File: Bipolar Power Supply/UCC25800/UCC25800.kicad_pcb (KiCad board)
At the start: 2 copper layers, 70 x 50 mm, 71 parts, among them J1 1715721, J2 1715734, T1 750319331, U1 UCC25800-Q1, U2 LT8330_S6, U4 LT8330_S6, U5 LM317EMPX/NOPB, U6 LM337IMPX/NOPB

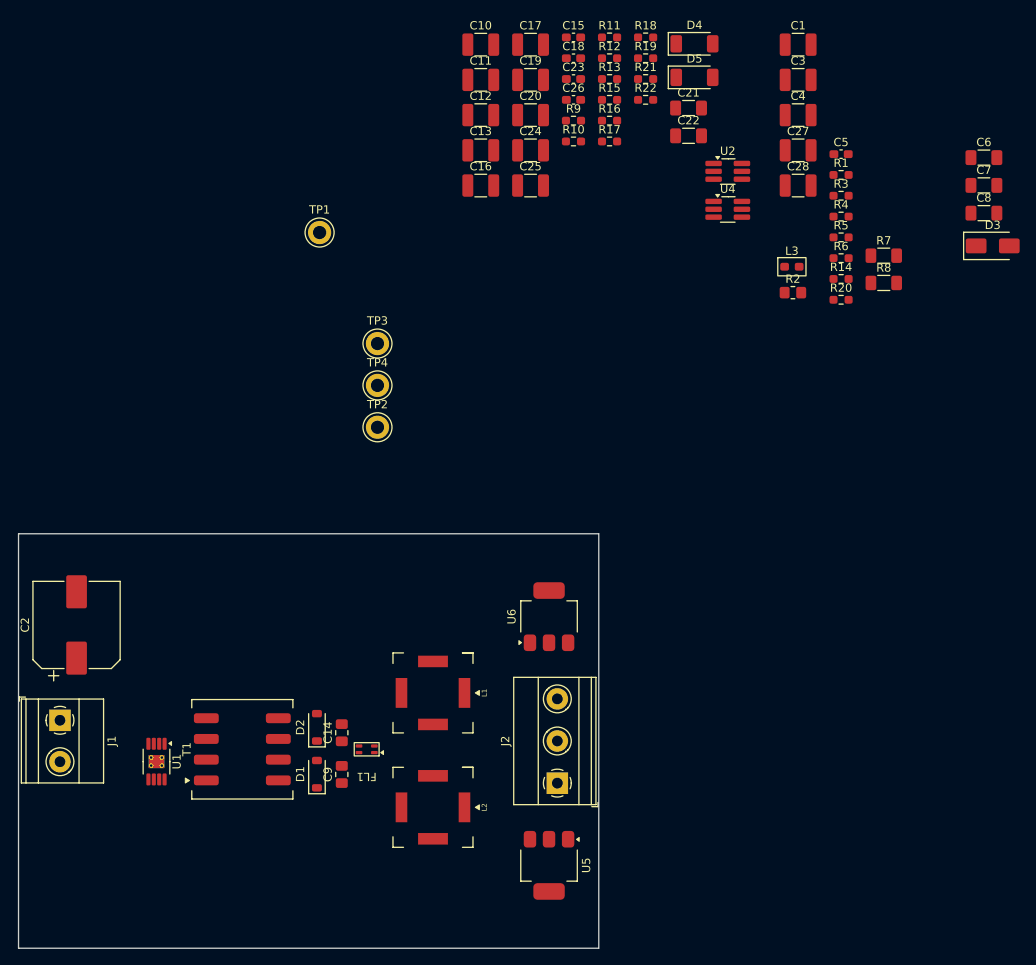
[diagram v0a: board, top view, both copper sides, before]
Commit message: UCC25800 : PCB layout
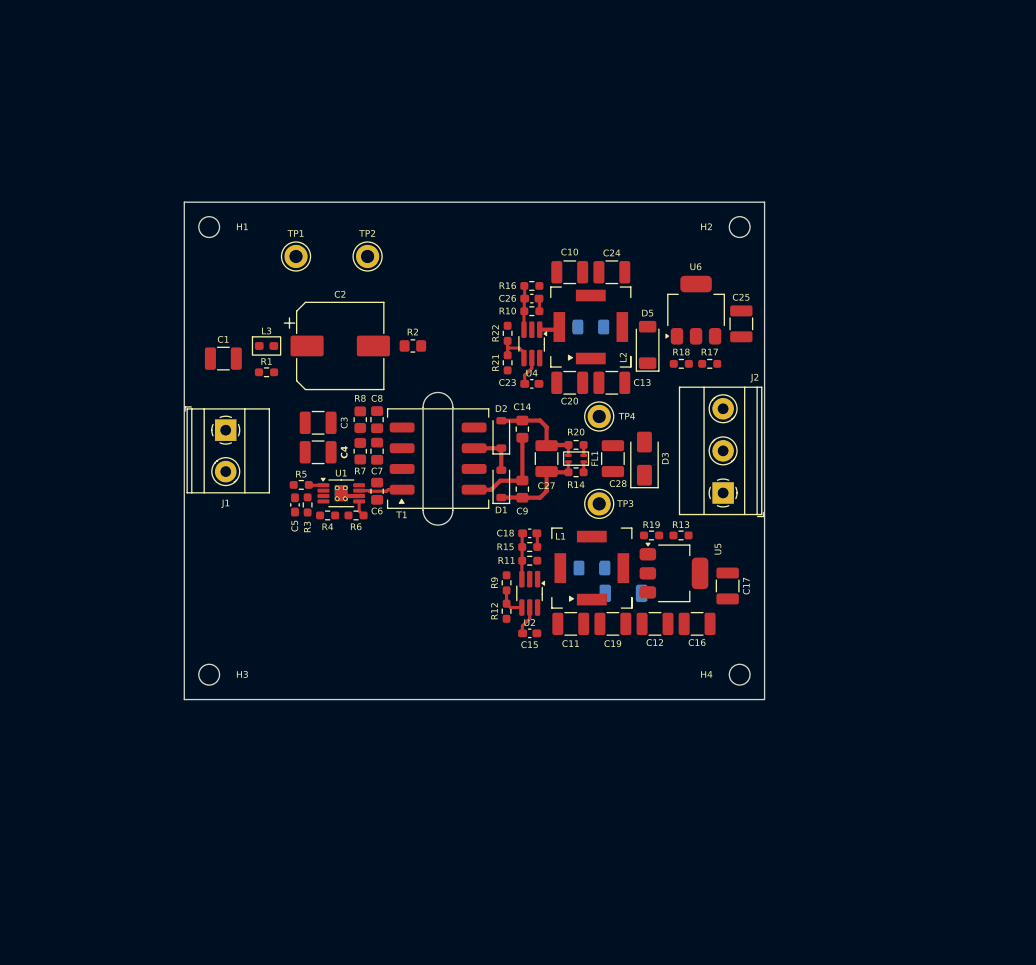
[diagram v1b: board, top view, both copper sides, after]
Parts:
- added H1: MountingHole, MountingHole:MountingHole_2.5mm, F.Cu at (123.0, 63.0)
- added H2: MountingHole, MountingHole:MountingHole_2.5mm, F.Cu at (187.0, 63.0)
- added H3: MountingHole, MountingHole:MountingHole_2.5mm, F.Cu at (123.0, 117.0)
- added H4: MountingHole, MountingHole:MountingHole_2.5mm, F.Cu at (187.0, 117.0)
- C21, C22, D4: moved to B.Cu
- C6, C7, C8: footprint Capacitor_SMD:C_1206_3216Metric_Pad1.33x1.80mm_HandSolder -> Capacitor_SMD:C_0805_2012Metric_Pad1.18x1.45mm_HandSolder
- R7, R8: footprint Resistor_SMD:R_1206_3216Metric_Pad1.30x1.75mm_HandSolder -> Resistor_SMD:R_0805_2012Metric_Pad1.20x1.40mm_HandSolder
- moved C6 83.5 mm to (143.3, 94.9), turned to -90 degrees
- moved C7 79.9 mm to (143.3, 90.0), turned to 90 degrees
- moved C1 79.0 mm to (124.7, 78.9), turned to 180 degrees
- moved C5 78.3 mm to (133.3, 96.5), turned to -90 degrees
- moved C8 77.3 mm to (143.3, 86.2), turned to 90 degrees
- moved R3 74.4 mm to (134.9, 96.5), turned to -90 degrees
- moved R1 73.3 mm to (129.9, 80.5)
- moved C15 72.1 mm to (161.7, 112.0)
- moved R4 71.7 mm to (137.3, 97.8)
- moved R5 71.6 mm to (134.1, 94.1)
- moved C3 71.2 mm to (136.1, 86.6), turned to 180 degrees
- moved C4 70.8 mm to (136.1, 90.2), turned to 180 degrees
- moved C17 69.5 mm to (185.5, 106.3), turned to -90 degrees
- moved R12 67.9 mm to (158.9, 109.3), turned to 90 degrees
- moved R7 67.4 mm to (141.2, 90.0), turned to 90 degrees
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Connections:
- FL1 pad 1: GND -> +24V
- FL1 pad 2: +24V -> GND
- FL1 pad 3: Net-(D1-K) -> Net-(D2-A)
- FL1 pad 4: Net-(D2-A) -> Net-(D1-K)
- TP3 pad 1: Net-(D1-K) -> +24V
- TP4 pad 1: Net-(D2-A) -> GND
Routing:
- net Net-(D1-K): track 0.00 -> 12.1 mm
- net Net-(D2-A): track 0.00 -> 12.0 mm
- net Net-(T1-SB): track 0.00 -> 11.4 mm
- net Net-(D1-A): track 0.00 -> 5.95 mm
- net Net-(U2-FBX): track 0.00 -> 5.57 mm
- net Net-(U4-EN/UVLO): track 0.00 -> 5.54 mm
- net Net-(U4-FBX): track 0.00 -> 5.33 mm
- net Net-(T1-AA): track 0.00 -> 5.30 mm
- net Net-(U2-EN/UVLO): track 0.00 -> 3.64 mm
- net Net-(U2-INTVCC): track 0.00 -> 3.50 mm
- net Net-(U4-INTVCC): track 0.00 -> 3.47 mm
- net Net-(U4-SW): track 0.00 -> 2.50 mm
- net GNDS: track 0.00 -> 2.28 mm
- net Net-(U1-RT): track 0.00 -> 1.92 mm
- net Net-(U1-SYNC): track 0.00 -> 1.78 mm
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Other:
- board size 70 x 50 mm -> 70 x 60 mm

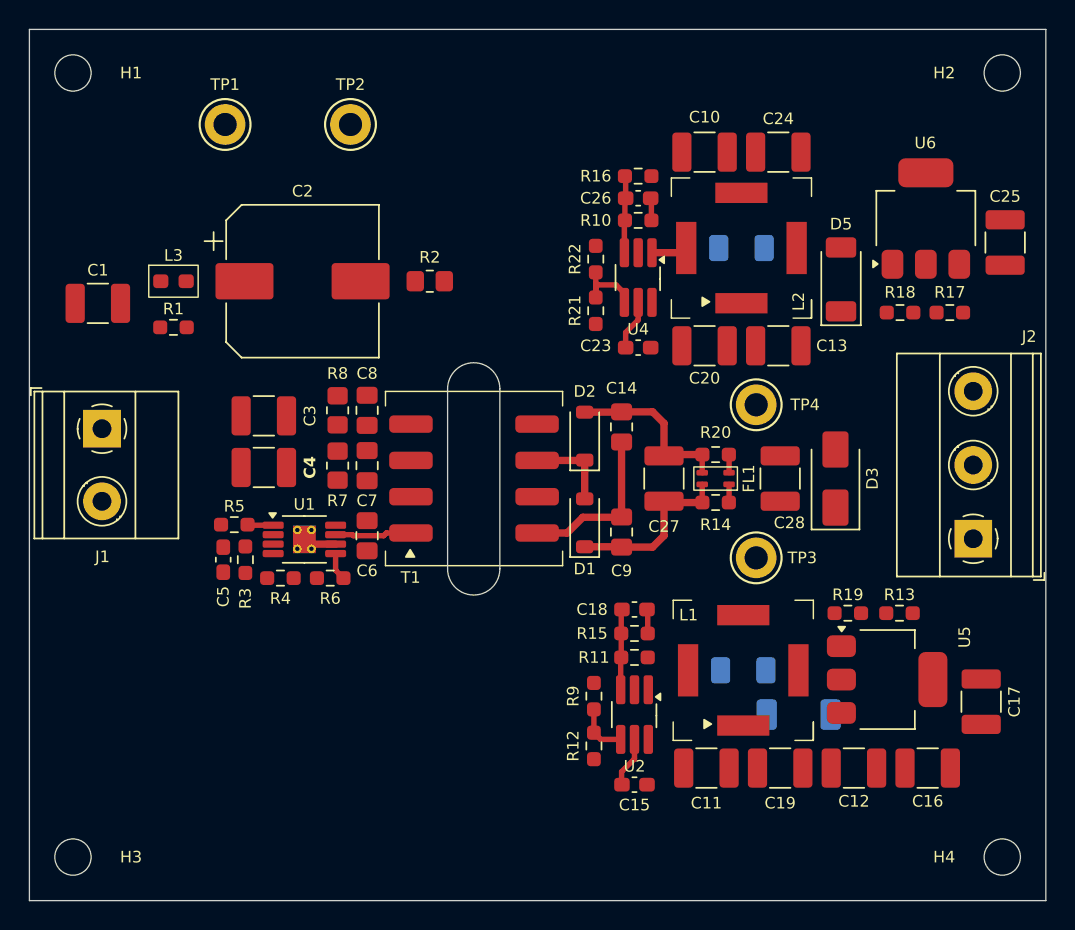
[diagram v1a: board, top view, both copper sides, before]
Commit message: BOOST_LT8365 : Design for bipolar 110V supply
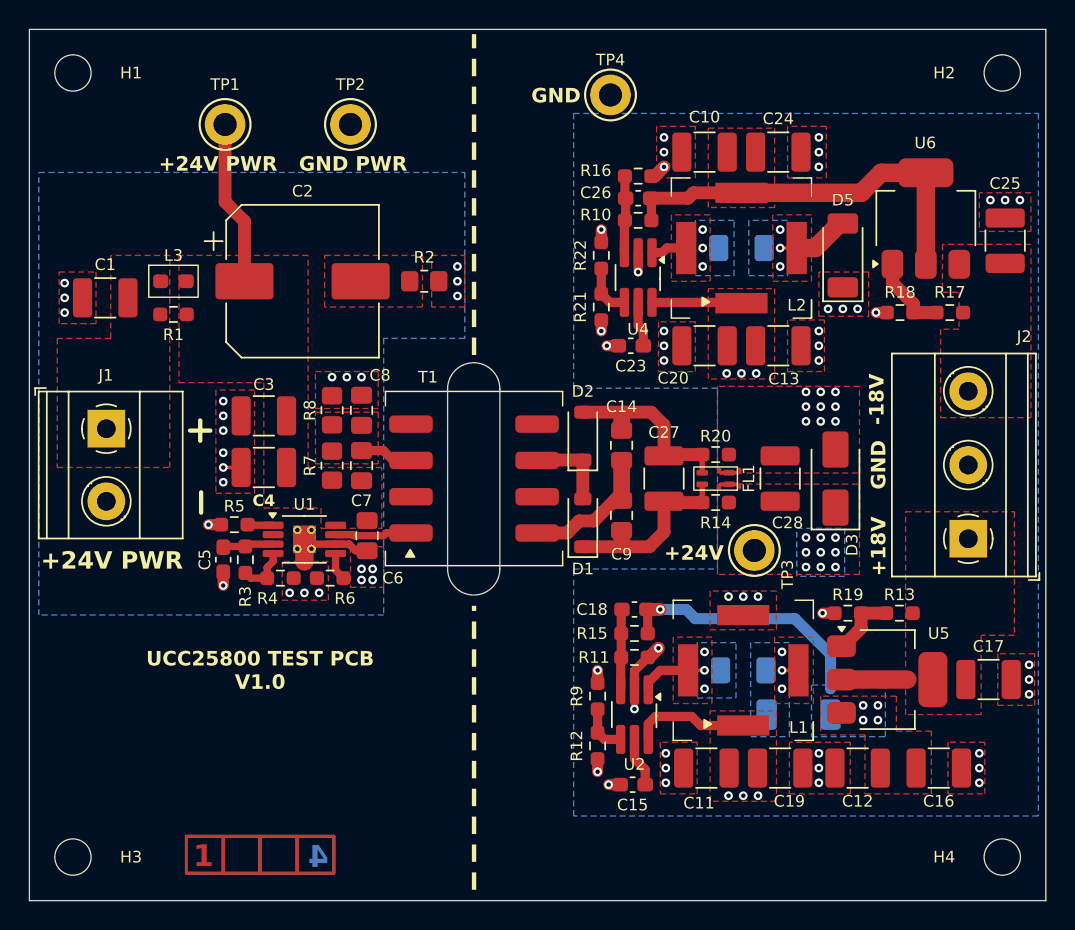
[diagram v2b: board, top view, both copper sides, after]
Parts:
- L3: value 0603PS-SRF -> 0603AF-241XJRW
- R3: value 24k9 -> 4k99
- R4: value 22k9 -> 4k99
- moved TP4 23.6 mm to (160.0, 64.5)
- moved D5 1.66 mm to (176.0, 75.6)
- moved C17 1.61 mm to (186.1, 104.8), turned to 0 degrees
- moved C14 1.27 mm to (160.8, 88.6)
- moved C9 1.14 mm to (160.8, 93.5)
- moved R1 0.89 mm to (129.9, 79.6)
- moved C16 0.76 mm to (182.6, 110.9)
- moved C1 0.63 mm to (125.2, 78.5)
- moved C23 0.52 mm to (161.4, 81.8), turned to 180 degrees
- moved TP3 0.52 mm to (169.9, 95.9)
- moved R21 0.46 mm to (159.4, 79.1)
- moved R22 0.46 mm to (159.4, 75.6)
- moved C7 0.38 mm to (142.9, 90.0)
- moved C8 0.38 mm to (142.9, 86.2)
- moved R2 0.38 mm to (147.2, 77.3)
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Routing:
- net Net-(U6-VI): track 1.54 -> 27.5 mm
- net GNDS: track 2.28 -> 26.1 mm, vias 0 -> 24
- net GND: track 1.26 -> 21.3 mm, vias 0 -> 51
- net +24V: track 1.26 -> 17.6 mm, vias 0 -> 17
- net Net-(D4-K): track 1.67 -> 18.0 mm, vias 0 -> 5
- net Net-(U1-VCC): track 0.05 -> 11.8 mm
- net Net-(U6-ADJ): track 0.00 -> 5.53 mm
- net Net-(D5-A): track 0.00 -> 5.02 mm, vias 0 -> 3
- net Net-(U2-SW): track 0.00 -> 4.86 mm, vias 0 -> 3
- net Net-(U5-ADJ): track 0.00 -> 4.63 mm
- net +18V: track 0.00 -> 4.55 mm
- net Net-(T1-AB): track 0.00 -> 3.68 mm
- net Net-(U1-VREG): track 0.00 -> 3.52 mm
- net Net-(U1-OC/DT): track 0.00 -> 3.51 mm
- net Net-(T1-SB): track 11.4 -> 9.50 mm
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- added copper zone on F.Cu, net +18V
- added copper zone on B.Cu, net +24V
- added copper zone on F.Cu, net +24V
- added copper zone on In1.Cu, net +24V
- added copper zone on In2.Cu, net +24V
- added copper zone on F.Cu, net -18V
- added copper zone on B.Cu, net GND
- added copper zone on F.Cu, net GND
- added copper zone on In1.Cu, net GND
- added copper zone on B.Cu, net GNDS
- added copper zone on F.Cu, net GNDS
- added copper zone on In1.Cu, net GNDS
- added copper zone on In2.Cu, net GNDS
- added copper zone on F.Cu, net Net-(C2-Pad2)
- added copper zone on B.Cu, net Net-(D4-A)
- added copper zone on F.Cu, net Net-(D4-A)
- added copper zone on B.Cu, net Net-(D4-K)
- added copper zone on F.Cu, net Net-(D4-K)
- added copper zone on B.Cu, net Net-(D5-A)
- added copper zone on F.Cu, net Net-(D5-A)
- added copper zone on F.Cu, net Net-(J1-Pin_1)
- added copper zone on F.Cu, net Net-(T1-AB)
- added copper zone on F.Cu, net Net-(U1-VCC)
- added copper zone on B.Cu, net Net-(U2-SW)
- added copper zone on F.Cu, net Net-(U2-SW)
- added copper zone on B.Cu, net Net-(U4-SW)
- added copper zone on F.Cu, net Net-(U4-SW)
- added copper zone on F.Cu, net Net-(U6-VI)
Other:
- copper layers 2 -> 4
- board text added: "+18V"
- board text added: "+24V"
- board text added: "+24V PWR"
- board text added: "-18V"
- board text added: "1"
- board text added: "2"
- board text added: "3"
- board text added: "4"
- board text added: "GND"
- board text added: "GND PWR"
- board text added: "UCC25800 TEST PCB V1.0"
